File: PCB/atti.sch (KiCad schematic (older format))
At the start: 4 parts

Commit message: Preliminary subdesign
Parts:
- removed J?: USB_C_Receptacle, symbol Connector:USB_C_Receptacle
- added C? (x3): C_Small, symbol Device:C_Small
- added C? (x6): 100 nF, symbol Device:C_Small
- added D? (x2): LED, symbol Device:LED
- added R?: 200 kO, symbol Device:R_Small
- added U?: AP2112K-3.3, Package_TO_SOT_SMD:SOT-23-5, symbol Regulator_Linear:AP2112K-3.3
- added U?: NVT2006, symbol AsymLevelShifters:NVT2006
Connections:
- net SPI1_MISO: now reaches U?.1 (SDO)
- net SPI1_MISO: now also U?.12 (PA6), U?.5 (SDO)
- net BMX_CSB: now reaches U?.12 (CSB)
- net SPI1_SCK: now reaches U?.13 (SCX)
- net SPI1_SCK: now also U?.11 (PA5), U?.4 (SCK)
- net SPI1_MOSI: now reaches U?.14 (SDX)
- net SPI1_MOSI: now also U?.13 (PA7), U?.3 (SDI)
- net GND: now reaches U?.2 (GND)
- net GND: now also U?.1 (GND), U?.16 (VSS), U?.3 (GND), U?.32 (VSS), U?.6 (GNDIO), U?.7 (GND), U?.7 (GND), C?.1, C?.2, C?.2, C?.2, C?.2, C?.2, C?.2, C?.2, C?.2, U?.1 (GND), U?.2 (GND)
- net VDD: now reaches U?.5 (VDDIO)
- net VDD: now also U?.1 (VDD), U?.17 (VDD), U?.5 (VDDA), U?.6 (VDDIO), U?.8 (VDD), U?.8 (VDD), C?.1, C?.1, C?.1, C?.1, C?.1, C?.1, C?.1, C?.2, R?.1, U?.5 (VOUT)
- net BMP_CSB: now reaches U?.2 (CSB)
- net USART1_TX: now reaches U?.19 (PA9)
- net USART1_TX: now also U?.12 (B3)
- net USART1_RX: now reaches U?.20 (PA10)
- net USART1_RX: now also U?.11 (B4)
- net USART1_CTS: now reaches U?.21 (PA11)
- net USART1_CTS: now also U?.10 (B5)
- net USART1_RTS_DE: now reaches U?.22 (PA12)
- net USART1_RTS_DE: now also U?.9 (B6)
- net I2C1_SCL: now reaches U?.29 (PB6)
- net I2C1_SCL: now also U?.14 (B1)
- net I2C1_SDA: now reaches U?.30 (PB7)
- net I2C1_SDA: now also U?.13 (B2)
- new net: R?.2, U?.15 (VREFB), U?.16 (EN)
- new net VIN: C?.1, U?.1 (VIN), U?.2 (VREFA)
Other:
- note added: "REGULATION"
- moved on the sheet: U?

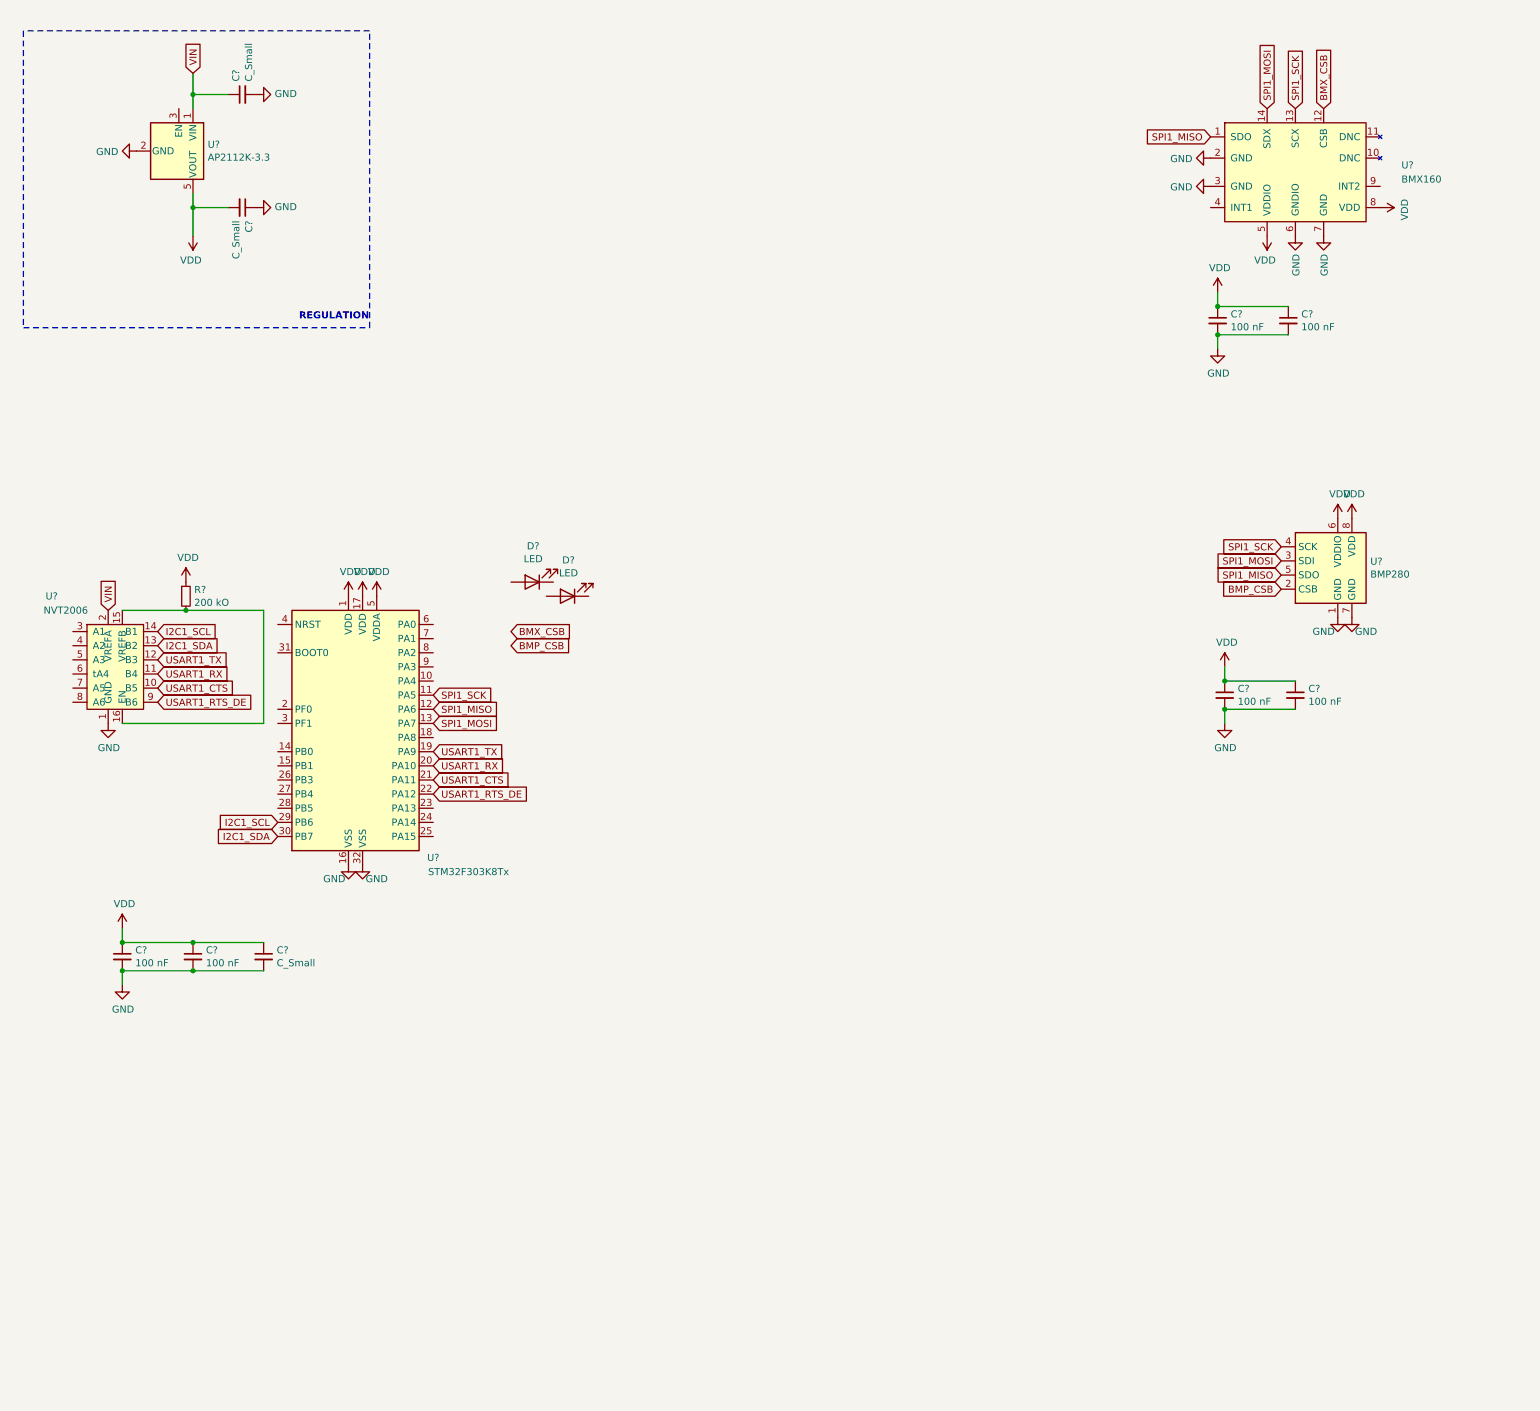
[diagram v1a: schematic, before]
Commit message: Add USB COM IC and various other routing work
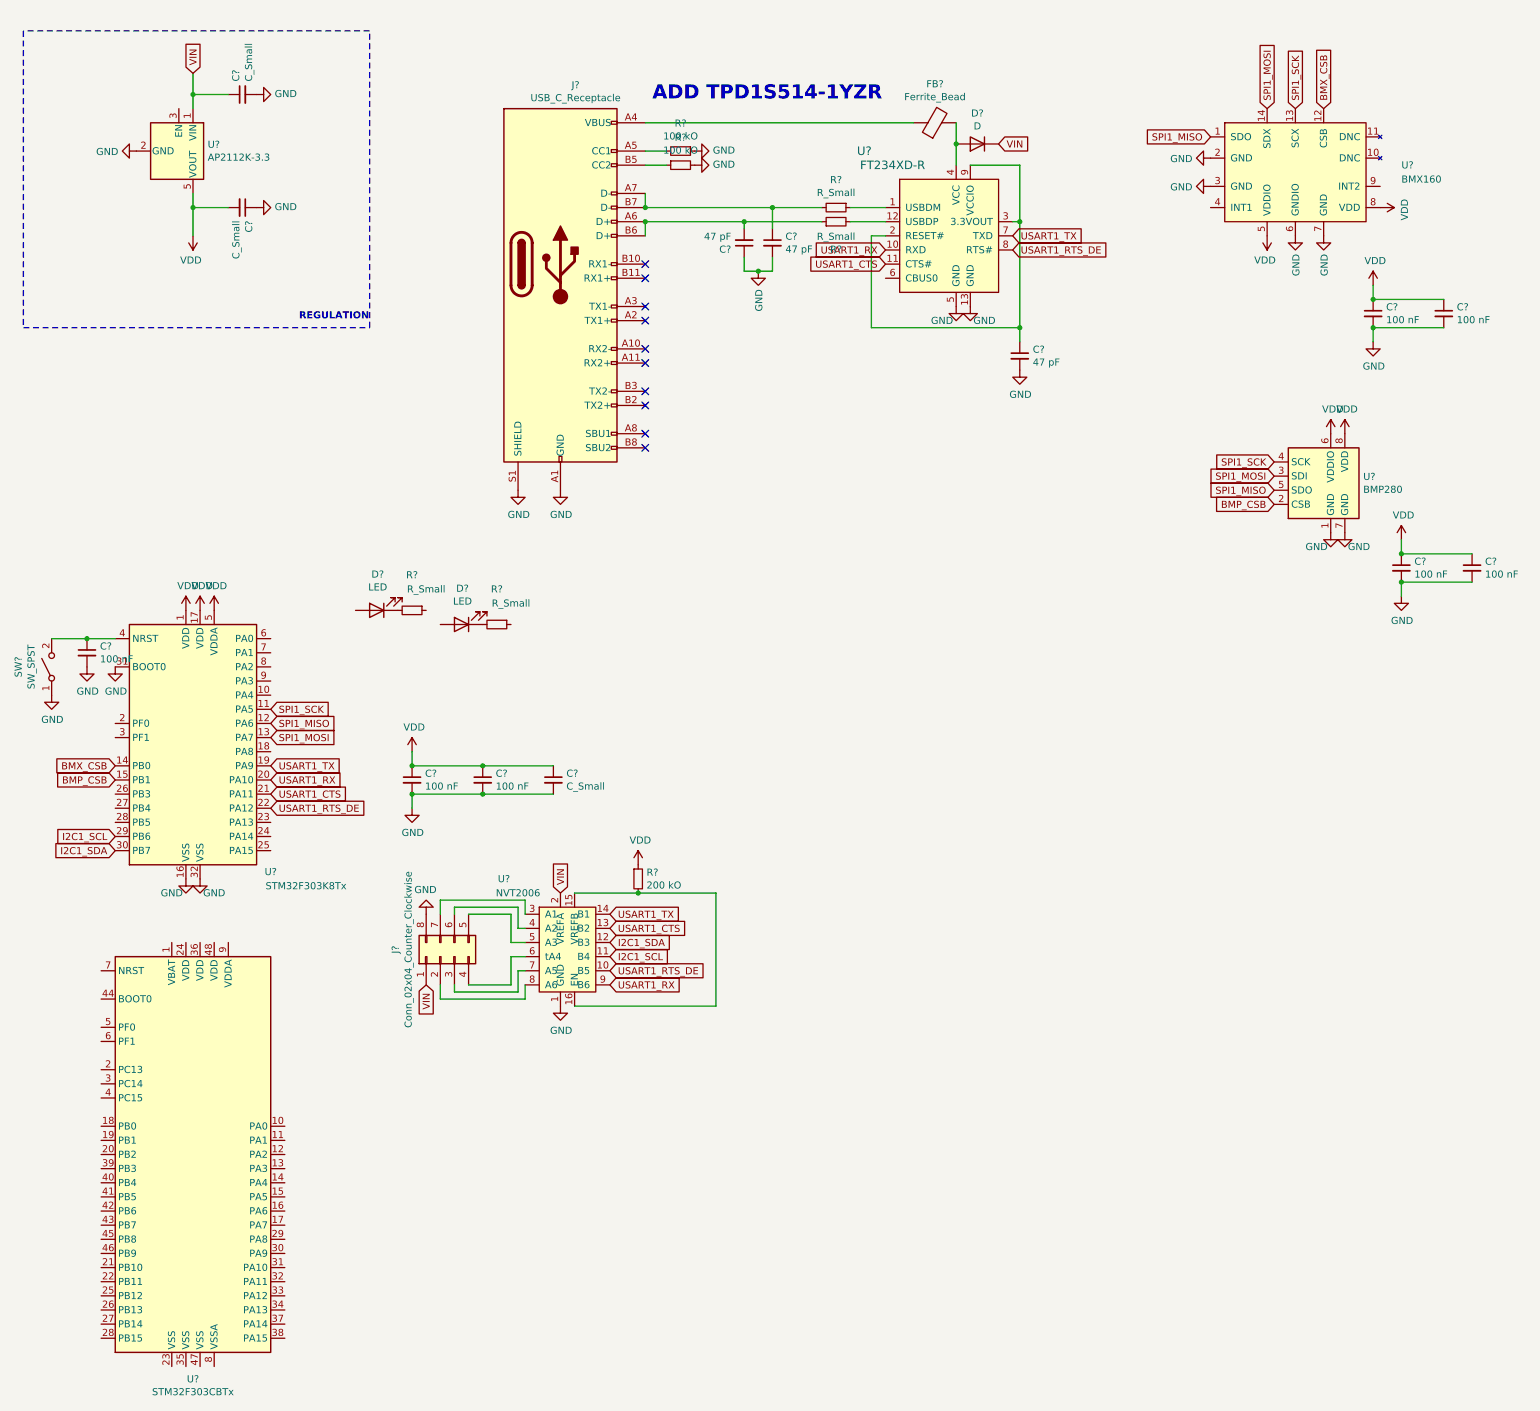
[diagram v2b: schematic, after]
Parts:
- removed D?: LED, symbol Device:LED
- added C? (x3): 47 pF, symbol Device:C_Small
- added C?: 100 nF, symbol Device:C_Small
- added D?: D, symbol Device:D
- added D?: LED, symbol Device:LED
- added FB?: Ferrite_Bead, symbol Device:Ferrite_Bead
- added J?: Conn_02x04_Counter_Clockwise, symbol Connector_Generic:Conn_02x04_Counter_Clockwise
- added J?: USB_C_Receptacle, symbol Connector:USB_C_Receptacle
- added R? (x4): R_Small, symbol Device:R_Small
- added R? (x2): 100 kO, symbol Device:R_Small
- added SW?: SW_SPST, symbol Switch:SW_SPST
- added U?: FT234XD-R, digikey-footprints:DFN-12-1EP_3x3mm, symbol dk_Interface-Controllers:FT234XD-R
- added U?: STM32F303CBTx, Package_QFP:LQFP-48_7x7mm_P0.5mm, symbol MCU_ST_STM32F3:STM32F303CBTx
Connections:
- net BMP_CSB: now also U?.15 (PB1)
- net BMX_CSB: now also U?.14 (PB0)
- net GND: now also U?.31 (BOOT0), C?.1, C?.2, C?.2, C?.2, J?.8 (Pin_8), J?.A1 (GND), J?.A12 (GND), J?.B1 (GND), J?.B12 (GND), J?.S1 (SHIELD), R?.1, R?.2, SW?.1 (A), U?.13 (GND), U?.5 (GND)
- net I2C1_SCL: now also U?.11 (B4); no longer U?.14 (B1)
- net I2C1_SDA: now also U?.12 (B3); no longer U?.13 (B2)
- net USART1_CTS: now also U?.13 (B2), U?.11 (CTS#); no longer U?.10 (B5)
- net USART1_RTS_DE: now also U?.10 (B5), U?.8 (RTS#); no longer U?.9 (B6)
- net USART1_RX: now also U?.9 (B6), U?.10 (RXD); no longer U?.11 (B4)
- net USART1_TX: now also U?.14 (B1), U?.7 (TXD); no longer U?.12 (B3)
- net VIN: now also D?.1 (K), J?.1 (Pin_1)
- net at U?.4 (NRST): now also C?.1, SW?.2 (B)
- net at U?.3 (A1): now also J?.7 (Pin_7)
- net at U?.4 (A2): now also J?.6 (Pin_6)
- net at U?.5 (A3): now also J?.5 (Pin_5)
- net at U?.6 (tA4): now also J?.4 (Pin_4)
- net at U?.7 (A5): now also J?.3 (Pin_3)
- net at U?.8 (A6): now also J?.2 (Pin_2)
- net at D?.1 (K): now also R?.2
- new net: FB?.1, J?.A4 (VBUS), J?.A9 (VBUS), J?.B4 (VBUS), J?.B9 (VBUS)
- new net: D?.2 (A), FB?.2, U?.4 (VCC)
- new net: R?.1, U?.1 (USBDM)
- new net: C?.1, J?.A7 (D-), J?.B7 (D-), R?.2
- new net: C?.2, J?.A6 (D+), J?.B6 (D+), R?.1
- new net: R?.2, U?.12 (USBDP)
- new net: C?.1, U?.2 (RESET#), U?.3 (3.3VOUT), U?.9 (VCCIO)
- new net: D?.1 (K), R?.2
- new net: J?.A5 (CC1), R?.2
- new net: J?.B5 (CC2), R?.1
- no-connect marks 0 -> 10
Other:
- note added: "ADD TPD1S514-1YZR"
- moved on the sheet: C?, D?, R?, U?

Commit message: Finish preliminary schematic
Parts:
- removed C? (x3): 47 pF, symbol Device:C_Small
- removed D?: D, symbol Device:D
- removed FB?: Ferrite_Bead, symbol Device:Ferrite_Bead
- removed J?: USB_C_Receptacle, symbol Connector:USB_C_Receptacle
- removed R? (x2): R_Small, symbol Device:R_Small
- removed R? (x2): 100 kO, symbol Device:R_Small
- removed U?: FT234XD-R, digikey-footprints:DFN-12-1EP_3x3mm, symbol dk_Interface-Controllers:FT234XD-R
- removed U?: STM32F303CBTx, Package_QFP:LQFP-48_7x7mm_P0.5mm, symbol MCU_ST_STM32F3:STM32F303CBTx
- added C10, C9: 4 pF, Capacitor_SMD:C_0805_2012Metric, symbol Device:C_Small
- added C5: 10 nF, Capacitor_SMD:C_0805_2012Metric, symbol Device:C_Small
- added C7: 1 uF, Capacitor_SMD:C_0805_2012Metric, symbol Device:C_Small
- added J2, J3, J4, J5, J6, J7, J8, J9: Conn_01x01_Female, Connector_Wire:SolderWire-0.25sqmm_1x01_D0.65mm_OD1.7mm, symbol Connector:Conn_01x01_Female
- added R3: 620 R, Resistor_SMD:R_0805_2012Metric, symbol Device:R_Small_US
- added R4, R6: 10 kR, Resistor_SMD:R_0805_2012Metric, symbol Device:R_Small
- added Y1: 32 MHz, Crystal:Crystal_SMD_SeikoEpson_TSX3225-4Pin_3.2x2.5mm, symbol Device:Crystal_Small
- C1, C12, C13, C14, C15, C4, C6: renamed from C?; footprint (none) -> Capacitor_SMD:C_0805_2012Metric
- C2, C3: renamed from C?; value C_Small -> 1 uF; footprint (none) -> Capacitor_SMD:C_0805_2012Metric
- C8: renamed from C?; value C_Small -> 4.7 uF; footprint (none) -> Capacitor_SMD:C_0805_2012Metric
- D1: renamed from D?; value LED -> LED_GREEN; footprint (none) -> LED_SMD:LED_0805_2012Metric
- D2: renamed from D?; value LED -> LED_RED; footprint (none) -> LED_SMD:LED_0805_2012Metric
- J1: renamed from J?; footprint (none) -> Connector_PinHeader_2.54mm:PinHeader_2x04_P2.54mm_Vertical
- R1, R2: renamed from R?; value R_Small -> 68 R; footprint (none) -> Resistor_SMD:R_0805_2012Metric
- R5: renamed from R?; value 200 kO -> 200 kR; footprint (none) -> Resistor_SMD:R_0805_2012Metric
- SW1: renamed from SW?; footprint (none) -> Button_Switch_SMD:SW_SPST_PTS810
- U3: renamed from U?; footprint (none) -> Package_SO:TSSOP-16_4.4x5mm_P0.65mm
- U5: renamed from U?; footprint (none) -> Package_LGA:Bosch_LGA-14_3x2.5mm_P0.5mm
- gave numbers to parts that had none: 3
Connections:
- net GND: now also R1.1, R2.1, C10.2, C5.2, C7.2, C9.2
- net I2C1_SCL: now also R6.2
- net I2C1_SDA: now also R4.1
- net VDD: now also C5.1, C7.1, R4.2, R6.1
- net VIN: now also U1.3 (EN)
- net BMX_INT1: now reaches U5.4 (INT1)
- net BMX_INT1: now also U2.18 (PA8)
- net BMX_INT2: now reaches U5.9 (INT2)
- net BMX_INT2: now also U2.23 (PA13)
- net at U2.10 (PA4): now also J7.1 (Pin_1)
- net OSC_IN: now reaches U2.2 (PF0)
- net OSC_IN: now also C9.1, Y1.2
- net at U2.24 (PA14): now also J8.1 (Pin_1)
- net at U2.25 (PA15): now also J9.1 (Pin_1)
- net at U2.26 (PB3): now also J2.1 (Pin_1)
- net at U2.27 (PB4): now also J3.1 (Pin_1)
- net at U2.28 (PB5): now also J4.1 (Pin_1)
- net OSC_OUT: now reaches U2.3 (PF1)
- net OSC_OUT: now also R3.2
- net at U2.6 (PA0): now also D2.2 (A)
- net at U2.7 (PA1): now also D1.2 (A)
- net at U2.8 (PA2): now also J5.1 (Pin_1)
- net at U2.9 (PA3): now also J6.1 (Pin_1)
- new net: C10.1, R3.1, Y1.1
- no-connect marks 10 -> 0
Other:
- note removed: "ADD TPD1S514-1YZR"
- moved on the sheet: C1, C4, C6, C8, D1, D2, J1, R1, R2, R5, SW1, U2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

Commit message: Partial routing attempt and programming connector
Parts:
- removed J2, J4, J8, J9: Conn_01x01_Female, Connector_Wire:SolderWire-0.25sqmm_1x01_D0.65mm_OD1.7mm, symbol Connector:Conn_01x01_Female
- removed Y1: 32 MHz, Crystal:Crystal_SMD_SeikoEpson_TSX3225-4Pin_3.2x2.5mm, symbol Device:Crystal_Small
- added J2: FTSH-105-01-X-D-007-K, AsymConnectors:SAMTEC_FTSH-105-01-X-D-007-K, symbol AsymConnectors:FTSH-105-01-X-D-007-K
- added Y1: 32 MHz, Crystal:Crystal_SMD_SeikoEpson_TSX3225-4Pin_3.2x2.5mm, symbol Device:Crystal_GND24_Small
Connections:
- net BMX_INT2: now also U2.28 (PB5); no longer U2.23 (PA13)
- net GND: now also J2.3, J2.5, Y1.2, Y1.4
- net OSC_IN: now also Y1.3
- net VDD: now also J2.1
- net SWCLK: now reaches U2.24 (PA14)
- net SWCLK: now also J2.4
- net JTDI: now reaches U2.25 (PA15)
- net JTDI: now also J2.8
- net SWO: now reaches U2.26 (PB3)
- net SWO: now also J2.6
- net NRST: now reaches C1.1, SW1.2 (B), U2.4 (NRST)
- net NRST: now also J2.10
- net at C10.1, R3.1: now also Y1.1
- new net SWDIO: J2.2, U2.23 (PA13)
- no-connect marks 0 -> 1
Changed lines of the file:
@@
 Text GLabel 2850 5500 2    50   Input ~ 0
 BMX_INT1
-Text GLabel 2850 6000 2    50   Input ~ 0
-BMX_INT2
 $Comp
 L AsymLevelShifters:NVT2006 U3
@@
 Wire Wire Line
 	3100 4800 3100 4900
-$Comp
-L Device:Crystal_Small Y1
-U 1 1 5FE3AFDC
-P 1850 3600
-F 0 "Y1" V 1896 3512 50  0000 R CNN
-F 1 "32 MHz" V 1805 3512 50  0000 R CNN
-F 2 "Crystal:Crystal_SMD_SeikoEpson_TSX3225-4Pin_3.2x2.5mm" H 1850 3600 50  0001 C CNN
-F 3 "~" H 1850 3600 50  0001 C CNN
-	1    1850 3600
-	0    -1   -1   0
-$EndComp
 Text GLabel 1750 5300 0    50   Input ~ 0
 OSC_IN
@@
 	2850 4800 3100 4800
 $Comp
-L Connector:Conn_01x01_Female J2
-U 1 1 5FE07EBD
-P 1550 5800
-F 0 "J2" H 1578 5826 50  0000 L CNN
-F 1 "Conn_01x01_Female" H 1578 5735 50  0000 L CNN
-F 2 "Connector_Wire:SolderWire-0.25sqmm_1x01_D0.65mm_OD1.7mm" H 1550 5800 50  0001 C CNN
-F 3 "~" H 1550 5800 50  0001 C CNN
-	1    1550 5800
-	-1   0    0    1
-$EndComp
-$Comp
 L Connector:Conn_01x01_Female J3
 U 1 1 5FE09C11
@@
 $EndComp
 $Comp
-L Connector:Conn_01x01_Female J4
-U 1 1 5FE0B773
-P 1550 6000
-F 0 "J4" H 1578 6026 50  0000 L CNN
-F 1 "Conn_01x01_Female" H 1578 5935 50  0000 L CNN
-F 2 "Connector_Wire:SolderWire-0.25sqmm_1x01_D0.65mm_OD1.7mm" H 1550 6000 50  0001 C CNN
-F 3 "~" H 1550 6000 50  0001 C CNN
-	1    1550 6000
-	-1   0    0    1
-$EndComp
-$Comp
-L Connector:Conn_01x01_Female J8
-U 1 1 5FE36D10
-P 3050 6100
-F 0 "J8" H 3078 6126 50  0000 L CNN
-F 1 "Conn_01x01_Female" H 3078 6035 50  0000 L CNN
-F 2 "Connector_Wire:SolderWire-0.25sqmm_1x01_D0.65mm_OD1.7mm" H 3050 6100 50  0001 C CNN
-F 3 "~" H 3050 6100 50  0001 C CNN
-	1    3050 6100
-	1    0    0    -1
-$EndComp
-$Comp
-L Connector:Conn_01x01_Female J9
-U 1 1 5FE38A2A
-P 3050 6200
-F 0 "J9" H 3078 6226 50  0000 L CNN
-F 1 "Conn_01x01_Female" H 3078 6135 50  0000 L CNN
-F 2 "Connector_Wire:SolderWire-0.25sqmm_1x01_D0.65mm_OD1.7mm" H 3050 6200 50  0001 C CNN
-F 3 "~" H 3050 6200 50  0001 C CNN
-	1    3050 6200
-	1    0    0    -1
-$EndComp
+L Device:Crystal_GND24_Small Y1
+U 1 1 5FE91EF3
+P 1850 3600
+F 0 "Y1" V 1896 3456 50  0000 R CNN
+F 1 "32 MHz" V 1805 3456 50  0000 R CNN
+F 2 "Crystal:Crystal_SMD_SeikoEpson_TSX3225-4Pin_3.2x2.5mm" H 1850 3600 50  0001 C CNN
+F 3 "~" H 1850 3600 50  0001 C CNN
+	1    1850 3600
+	0    -1   -1   0
+$EndComp
+Wire Wire Line
+	1750 3600 1350 3600
+$Comp
+L power:GND #PWR?
+U 1 1 5FE9FB52
+P 1950 3600
+F 0 "#PWR?" H 1950 3350 50  0001 C CNN
+F 1 "GND" V 1955 3472 50  0000 R CNN
+F 2 "" H 1950 3600 50  0001 C CNN
+F 3 "" H 1950 3600 50  0001 C CNN
+	1    1950 3600
+	0    -1   -1   0
+$EndComp
+Text GLabel 1750 5800 0    50   Input ~ 0
+SWO
+Text GLabel 1750 6000 0    50   Input ~ 0
+BMX_INT2
+Text GLabel 2850 6000 2    50   Input ~ 0
+SWDIO
+Text GLabel 2850 6100 2    50   Input ~ 0
+SWCLK
+Text GLabel 1300 4700 1    50   Input ~ 0
+NRST
+Text GLabel 2850 6200 2    50   Input ~ 0
+JTDI
+Text GLabel 4950 2450 2    50   Input ~ 0
+SWDIO
+Text GLabel 4950 2550 2    50   Input ~ 0
+SWCLK
+Text GLabel 4950 2650 2    50   Input ~ 0
+SWO
+Text GLabel 4950 2750 2    50   Input ~ 0
+JTDI
+Text GLabel 4950 2850 2    50   Input ~ 0
+NRST
+$Comp
+L power:VDD #PWR?
+U 1 1 60088F29
+P 3950 2450
+F 0 "#PWR?" H 3950 2300 50  0001 C CNN
+F 1 "VDD" V 3965 2577 50  0000 L CNN
+F 2 "" H 3950 2450 50  0001 C CNN
+F 3 "" H 3950 2450 50  0001 C CNN
+	1    3950 2450
+	0    -1   -1   0
+$EndComp
+$Comp
+L power:GND #PWR?
+U 1 1 60089B95
+P 3950 2550
+F 0 "#PWR?" H 3950 2300 50  0001 C CNN
+F 1 "GND" V 3955 2422 50  0000 R CNN
+F 2 "" H 3950 2550 50  0001 C CNN
+F 3 "" H 3950 2550 50  0001 C CNN
+	1    3950 2550
+	0    1    1    0
+$EndComp
+$Comp
+L power:GND #PWR?
+U 1 1 6008A5E8
+P 3950 2650
+F 0 "#PWR?" H 3950 2400 50  0001 C CNN
+F 1 "GND" V 3955 2522 50  0000 R CNN
+F 2 "" H 3950 2650 50  0001 C CNN
+F 3 "" H 3950 2650 50  0001 C CNN
+	1    3950 2650
+	0    1    1    0
+$EndComp
+NoConn ~ 3950 2850
+$Comp
+L AsymConnectors:FTSH-105-01-X-D-007-K J2
+U 1 1 6009A82F
+P 4450 2650
+F 0 "J2" H 4450 3117 50  0000 C CNN
+F 1 "FTSH-105-01-X-D-007-K" H 4450 3026 50  0000 C CNN
+F 2 "AsymConnectors:SAMTEC_FTSH-105-01-X-D-007-K" H 4250 3200 50  0001 L BNN
+F 3 "" H 4700 2950 50  0001 L BNN
+F 4 "SAMTEC" H 4250 3100 50  0001 L BNN "MANUFACTURER"
+F 5 "B" H 4700 3000 50  0001 L BNN "PARTREV"
+F 6 "Manufacturer Recommendations" H 4250 3300 50  0001 L BNN "STANDARD"
+F 7 "5.7mm" H 4250 3000 50  0001 L BNN "MAXIMUM_PACKAGE_HEIGHT"
+	1    4450 2650
+	1    0    0    -1
+$EndComp

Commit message: Second routing attempt
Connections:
- net BMX_INT1: now also U2.27 (PB4); no longer U2.18 (PA8)
- net GND: now also J1.2 (Pin_2); no longer J1.8 (Pin_8)
- net I2C1_SCL: now also U3.10 (B5); no longer U3.11 (B4)
- net I2C1_SDA: now also U3.9 (B6); no longer U3.12 (B3)
- net USART1_CTS: now also U3.12 (B3); no longer U3.13 (B2)
- net USART1_RTS_DE: now also U3.11 (B4); no longer U3.10 (B5)
- net USART1_RX: now also U3.13 (B2); no longer U3.9 (B6)
- net at J3.1 (Pin_1): now also U2.18 (PA8); no longer U2.27 (PB4)
- net at U3.8 (A6): now also J1.3 (Pin_3); no longer J1.2 (Pin_2)
- net at U3.7 (A5): now also J1.4 (Pin_4); no longer J1.3 (Pin_3)
- net at U3.6 (tA4): now also J1.5 (Pin_5); no longer J1.4 (Pin_4)
- net at U3.5 (A3): now also J1.6 (Pin_6); no longer J1.5 (Pin_5)
- net at U3.4 (A2): now also J1.7 (Pin_7); no longer J1.6 (Pin_6)
- net at U3.3 (A1): now also J1.8 (Pin_8); no longer J1.7 (Pin_7)
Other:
- note added: "DEBUG"
- note added: "LEVEL SHIFTING"
- note added: "SENSORS"
- note added: "VDD DECOUPLING"
- note added: "VDDA DECOUPLING"
- moved on the sheet: C1, C10, C12, C13, C14, C15, C4, C5, C6, C7, C8, C9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
